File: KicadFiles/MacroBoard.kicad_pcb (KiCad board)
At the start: 2 copper layers, 7.5 x 2 mm, 79 parts, among them J1 USB_B_Micro, J2 Conn_01x08_Male, SW1 SW_Push, SW10 SW_Push, SW11 SW_Push, SW12 SW_Push, SW13 RotaryEncoder_Switch, SW14 SW_Push, SW15 SW_Push, SW16 SW_Push, SW17 SW_Push, SW2 SW_Push, SW3 SW_Push, SW4 SW_Push, SW5 SW_Push, SW6 SW_Push, SW7 SW_Push, SW8 SW_Push, SW9 SW_Push, U1 STM32F103C6Tx, U2 TC1262-33, Y1 8MHz

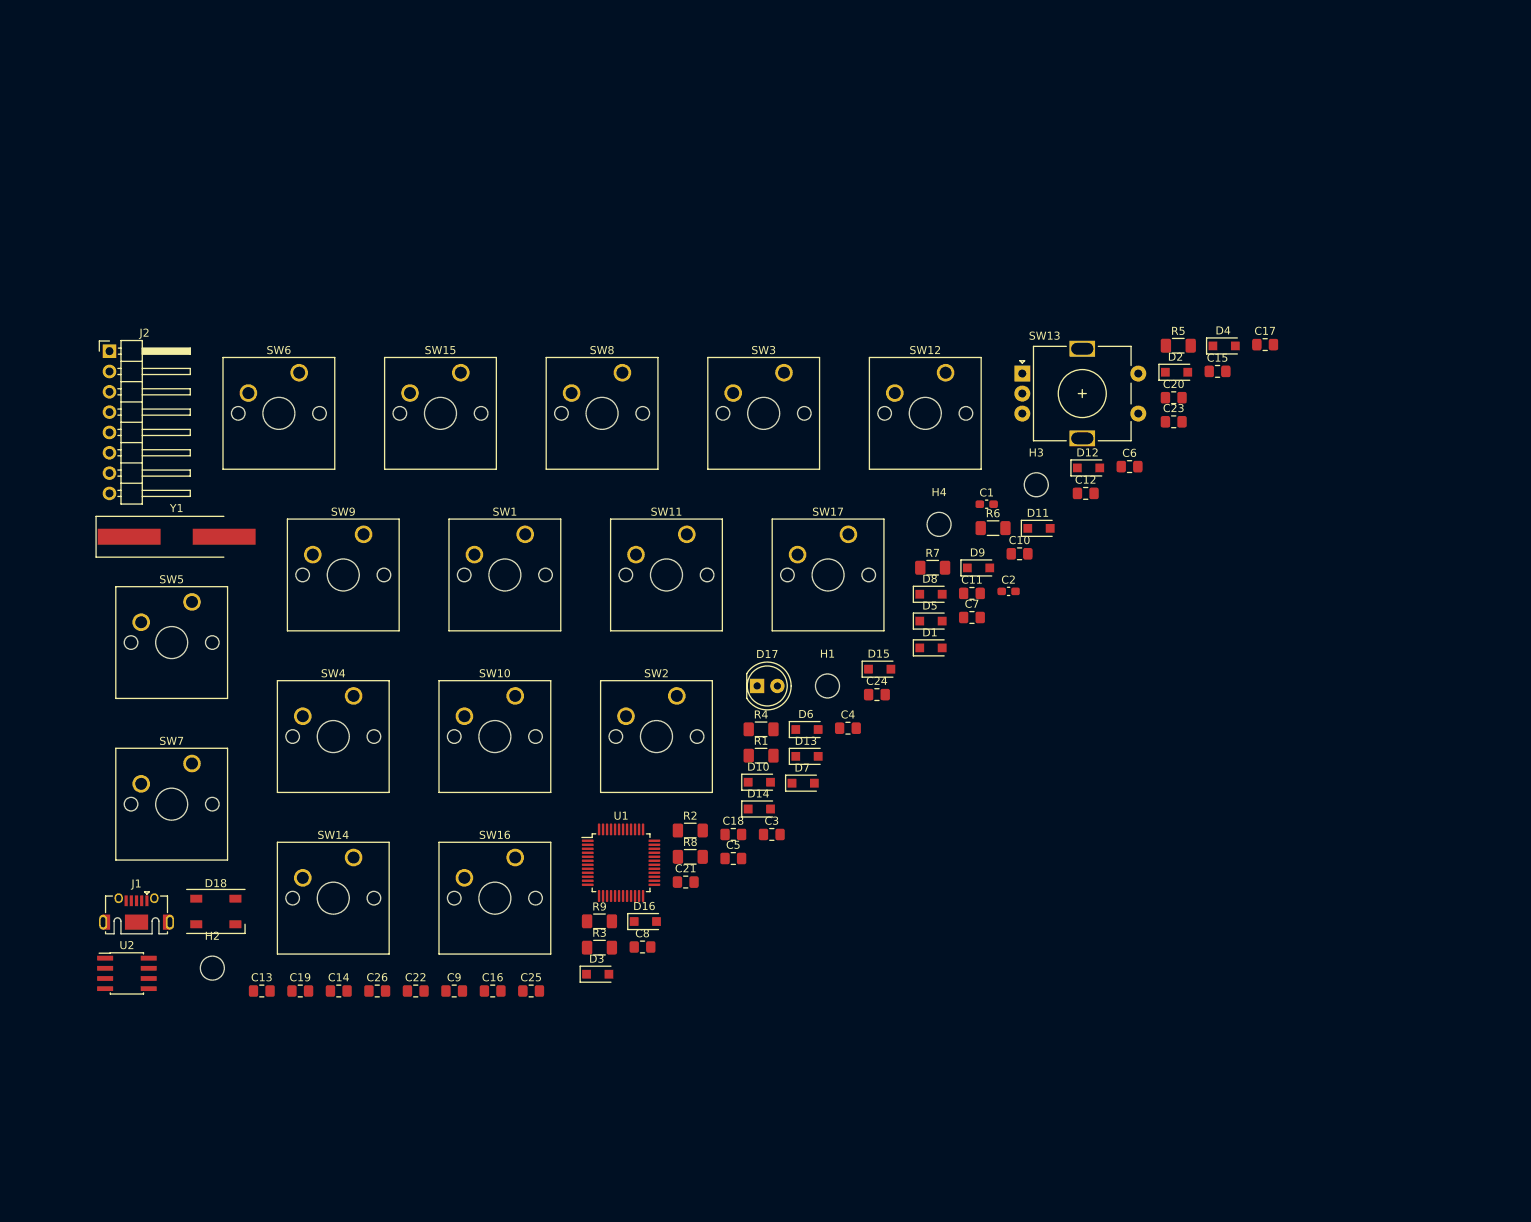
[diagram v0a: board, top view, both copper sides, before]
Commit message: pcb: arranged and connected switches with caps and diodes, everything else sucks
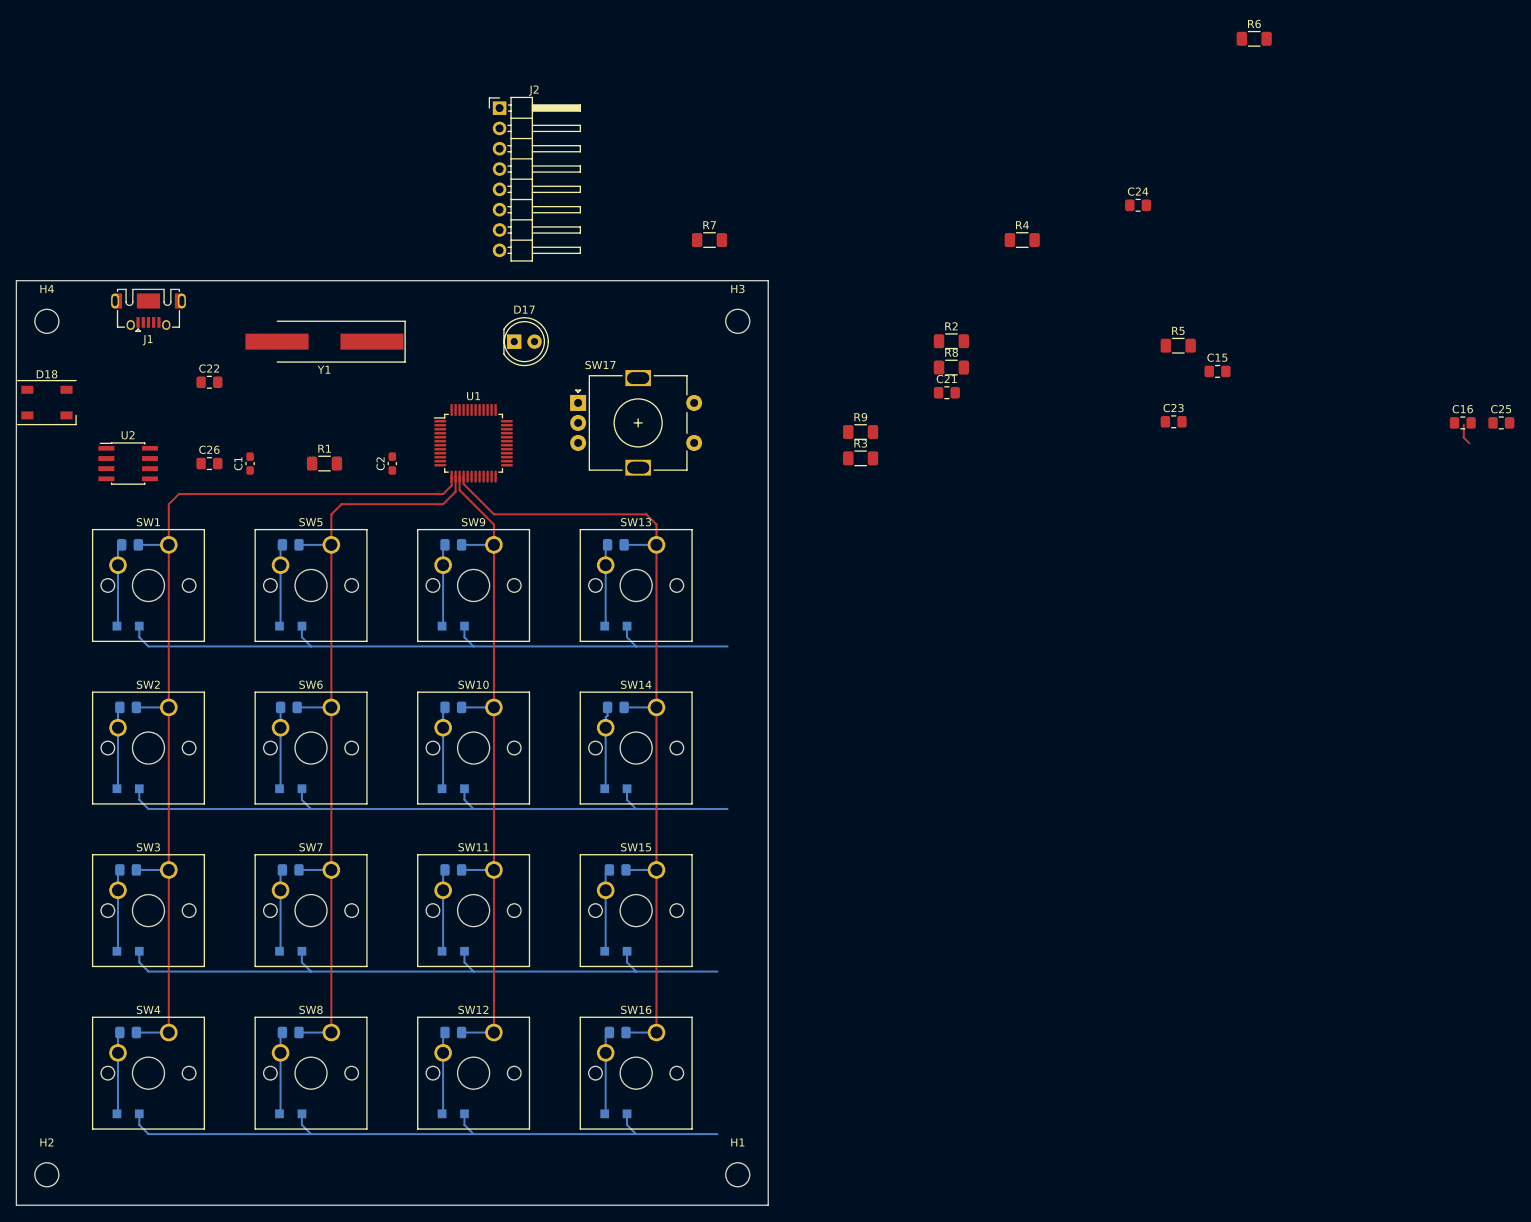
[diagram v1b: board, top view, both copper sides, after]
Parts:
- C10, C11, C12, C13, C14, C17, C18, C19, C20, C3, C4, C5, C6, C7, C8, C9, D1, D10, D11, D12, D13, D14, D15, D16, D2, D3, D4, D5, D6, D7, D8, D9: moved to B.Cu
- moved D4 167.3 mm to (30.5, 149.9), turned to 180 degrees
- moved C6 143.8 mm to (30.5, 139.7), turned to 180 degrees
- moved D2 141.0 mm to (30.5, 109.2), turned to 180 degrees
- moved C16 140.5 mm to (197.3, 63.5)
- moved C25 140.5 mm to (202.1, 63.5)
- moved H4 114.4 mm to (20.3, 50.8)
- moved D12 113.2 mm to (71.1, 149.9), turned to 180 degrees
- moved C10 109.0 mm to (50.8, 139.7), turned to 180 degrees
- moved C20 105.5 mm to (91.7, 139.7), turned to 180 degrees
- moved D8 103.1 mm to (50.8, 149.9), turned to 180 degrees
- moved D1 100.4 mm to (30.5, 88.9), turned to 180 degrees
- moved SW12 99.9 mm to (76.2, 139.7)
- moved SW3 98.9 mm to (35.6, 119.4)
- moved C1 92.2 mm to (45.7, 68.6), turned to 90 degrees
- moved D11 90.3 mm to (71.1, 129.5), turned to 180 degrees
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- renumbered SW14 to SW13, SW15 to SW14, SW16 to SW15, SW17 to SW16, SW13 to SW17
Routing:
- net COL0: track 0.00 -> 119.4 mm
- net COL3: track 0.00 -> 106.3 mm
- net COL1: track 0.00 -> 99.8 mm
- net COL2: track 0.00 -> 87.4 mm
- net ROW1: track 0.00 -> 84.4 mm
- net ROW0: track 0.00 -> 84.4 mm
- net ROW2: track 0.00 -> 83.2 mm
- net ROW3: track 0.00 -> 83.2 mm
- net Net-(C20-Pad2): track 0.00 -> 10.4 mm
- net Net-(C3-Pad2): track 0.00 -> 10.4 mm
- net Net-(C19-Pad2): track 0.00 -> 10.4 mm
- net Net-(C10-Pad2): track 0.00 -> 10.3 mm
- net Net-(C6-Pad2): track 0.00 -> 10.3 mm
- net Net-(C7-Pad2): track 0.00 -> 10.3 mm
- net Net-(C14-Pad2): track 0.00 -> 10.3 mm
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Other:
- board size 7.5 x 2 mm -> 94 x 115.6 mm

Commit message: connected rows and cols to MCU, gotto re-route it anyway because of the USB connectors being on the bad side
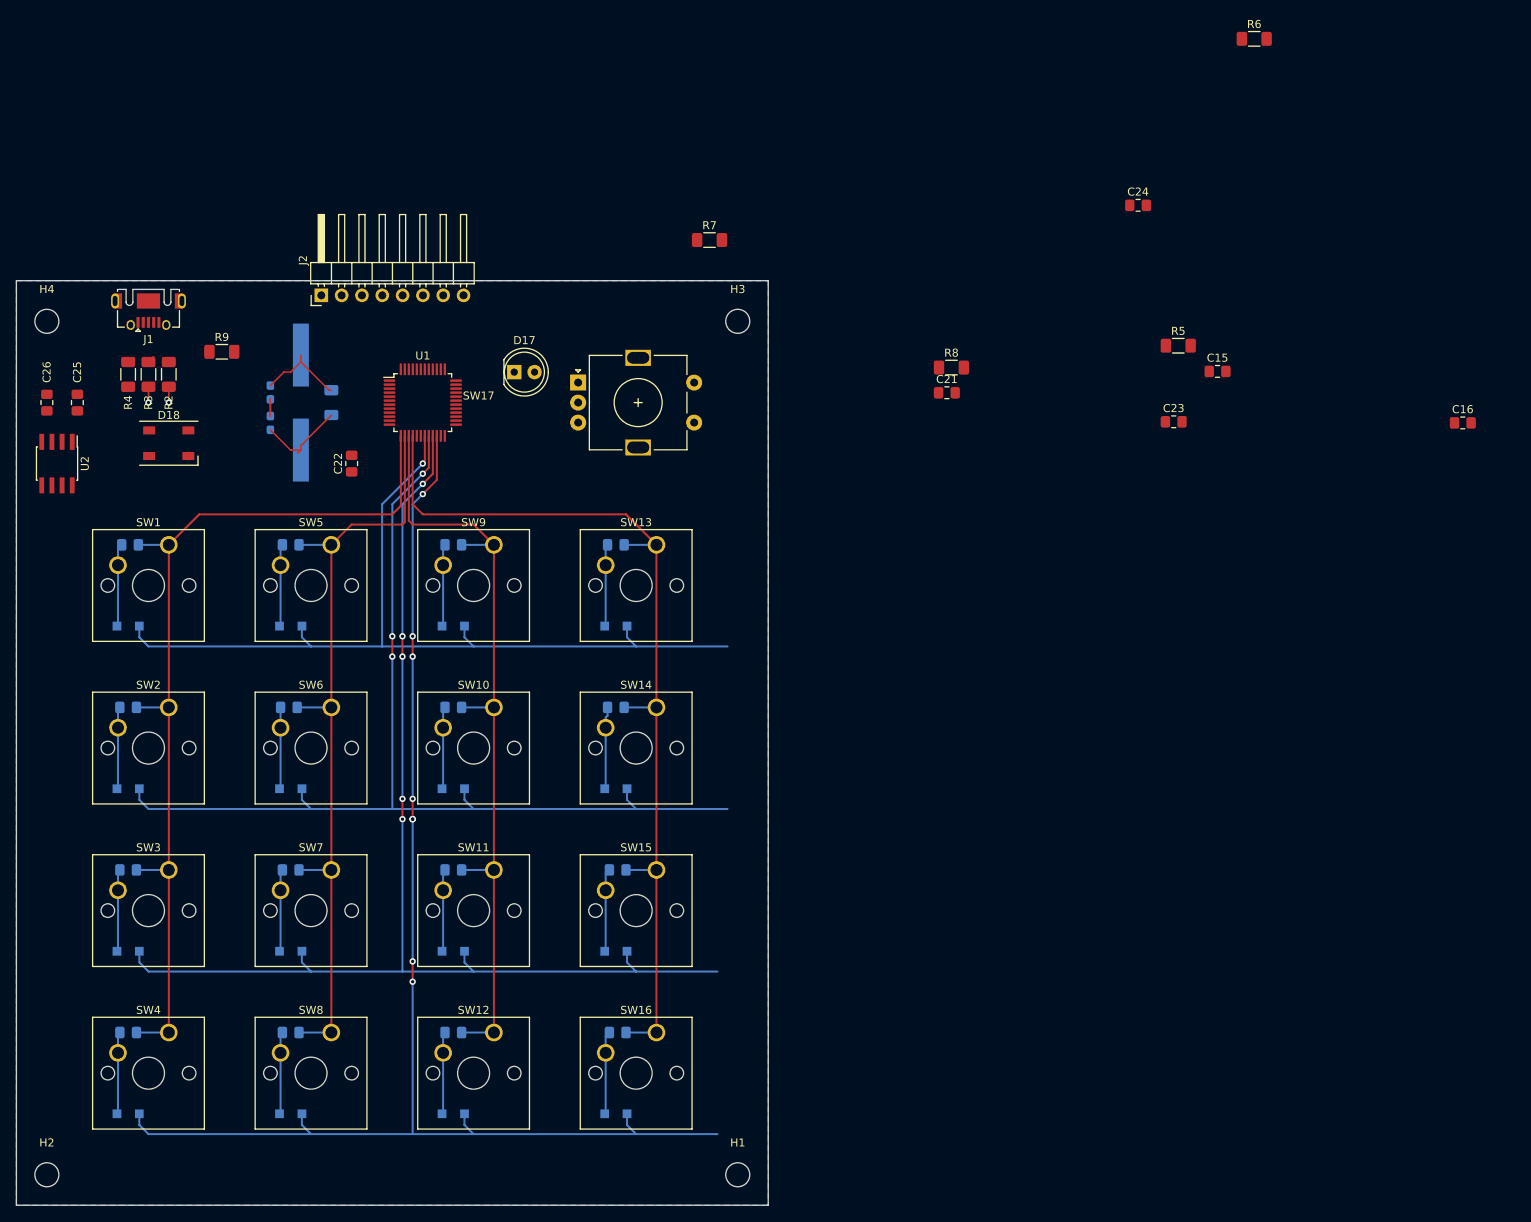
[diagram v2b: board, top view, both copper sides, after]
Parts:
- C1, C2, R1, Y1: moved to B.Cu
- moved C25 178.0 mm to (24.1, 61.0), turned to 90 degrees
- moved R4 113.0 mm to (30.5, 57.4), turned to -90 degrees
- moved R2 97.9 mm to (35.6, 57.4), turned to -90 degrees
- moved R3 89.6 mm to (33.0, 57.4), turned to 90 degrees
- moved R9 80.5 mm to (42.2, 54.6)
- moved J2 32.3 mm to (54.6, 47.6), turned to 90 degrees
- moved C26 21.7 mm to (20.3, 61.0), turned to 90 degrees
- moved C22 20.5 mm to (58.4, 68.6), turned to 90 degrees
- moved C2 17.6 mm to (48.3, 59.7)
- moved D18 16.1 mm to (35.6, 66.0)
- moved U2 8.89 mm to (21.6, 68.6), turned to -90 degrees
- moved Y1 8.17 mm to (52.1, 61.0), turned to -90 degrees
- moved U1 8.13 mm to (67.3, 61.0)
- moved R1 7.67 mm to (55.9, 61.0), turned to 90 degrees
- moved C1 5.68 mm to (48.3, 63.5), turned to -90 degrees
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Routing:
- net ROW3: track 83.2 -> 171.7 mm, vias 0 -> 8
- net ROW2: track 83.2 -> 151.7 mm, vias 0 -> 5
- net ROW1: track 84.4 -> 133.0 mm, vias 0 -> 3
- net ROW0: track 84.4 -> 113.0 mm, vias 0 -> 1
- net COL2: track 87.4 -> 99.6 mm
- net COL3: track 106.3 -> 117.8 mm
- net Crystal+: track 0.00 -> 11.4 mm
- net Crystal-: track 0.00 -> 11.2 mm
- net GND: track 0.00 -> 3.36 mm
- net COL0: track 119.4 -> 116.7 mm
- net (no net): track 2.59 -> 0.00 mm
- net USBD-: track 0.00 -> 1.98 mm, vias 0 -> 1
- net USBD+: track 0.00 -> 1.98 mm, vias 0 -> 1
- net COL1: track 99.8 -> 98.5 mm
- net Net-(J1-Pad2): track 0.00 -> 0.88 mm
- added copper zone on B.Cu, net GND

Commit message: stuff
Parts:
- U1: moved to B.Cu
- moved R6 108.1 mm to (76.2, 67.0), turned to 90 degrees
- moved R8 55.6 mm to (78.7, 67.0), turned to 90 degrees
- moved D18 41.6 mm to (76.2, 57.1), turned to 180 degrees
- moved R9 33.8 mm to (73.7, 67.0), turned to 90 degrees
- moved U1 23.4 mm to (44.5, 66.0), turned to 180 degrees
- moved C22 16.7 mm to (52.1, 53.1)
- moved D17 15.9 mm to (92.7, 49.5)
- moved Y1 13.1 mm to (64.8, 64.1), turned to 90 degrees
- moved C2 12.8 mm to (59.7, 65.3), turned to -90 degrees
- moved C1 11.6 mm to (59.7, 61.5), turned to 90 degrees
- moved R1 5.68 mm to (58.4, 55.9)
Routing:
- net led_green: track 0.00 -> 55.1 mm, vias 0 -> 1
- net led_blue: track 0.00 -> 50.7 mm, vias 0 -> 1
- net led_red: track 0.00 -> 46.4 mm, vias 0 -> 1
- net COL3: track 117.8 -> 76.7 mm
- net COL0: track 116.7 -> 76.9 mm
- net ROW0: track 113.0 -> 84.4 mm, vias 1 -> 0
- net ROW1: track 133.0 -> 106.0 mm, vias 3 -> 2
- net ROW2: track 151.7 -> 125.1 mm, vias 5 -> 4
- net ROW3: track 171.7 -> 145.4 mm, vias 8 -> 7
- net COL2: track 99.6 -> 77.1 mm
- net COL1: track 98.5 -> 77.4 mm
- net Net-(D18-Pad1): track 0.00 -> 12.1 mm
- net Crystal+: track 11.4 -> 0.00 mm
- net Crystal-: track 11.2 -> 0.00 mm
- net Net-(D18-Pad4): track 0.00 -> 10.9 mm
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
